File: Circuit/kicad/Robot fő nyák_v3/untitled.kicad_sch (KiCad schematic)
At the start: 0 parts

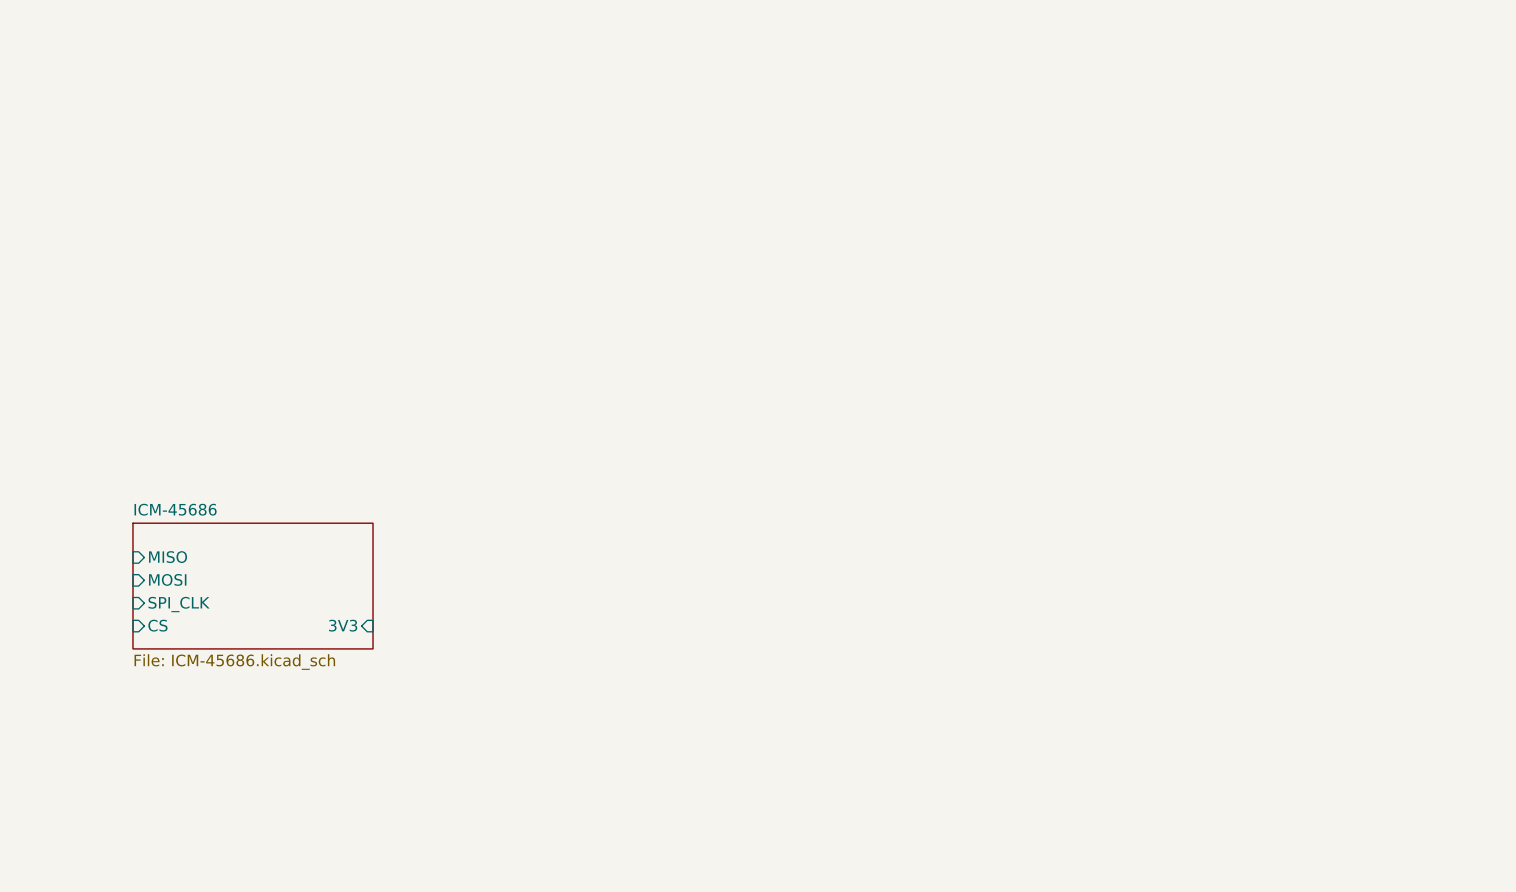
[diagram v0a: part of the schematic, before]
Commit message: kicad bugfixs + bno085 + level shifter ics
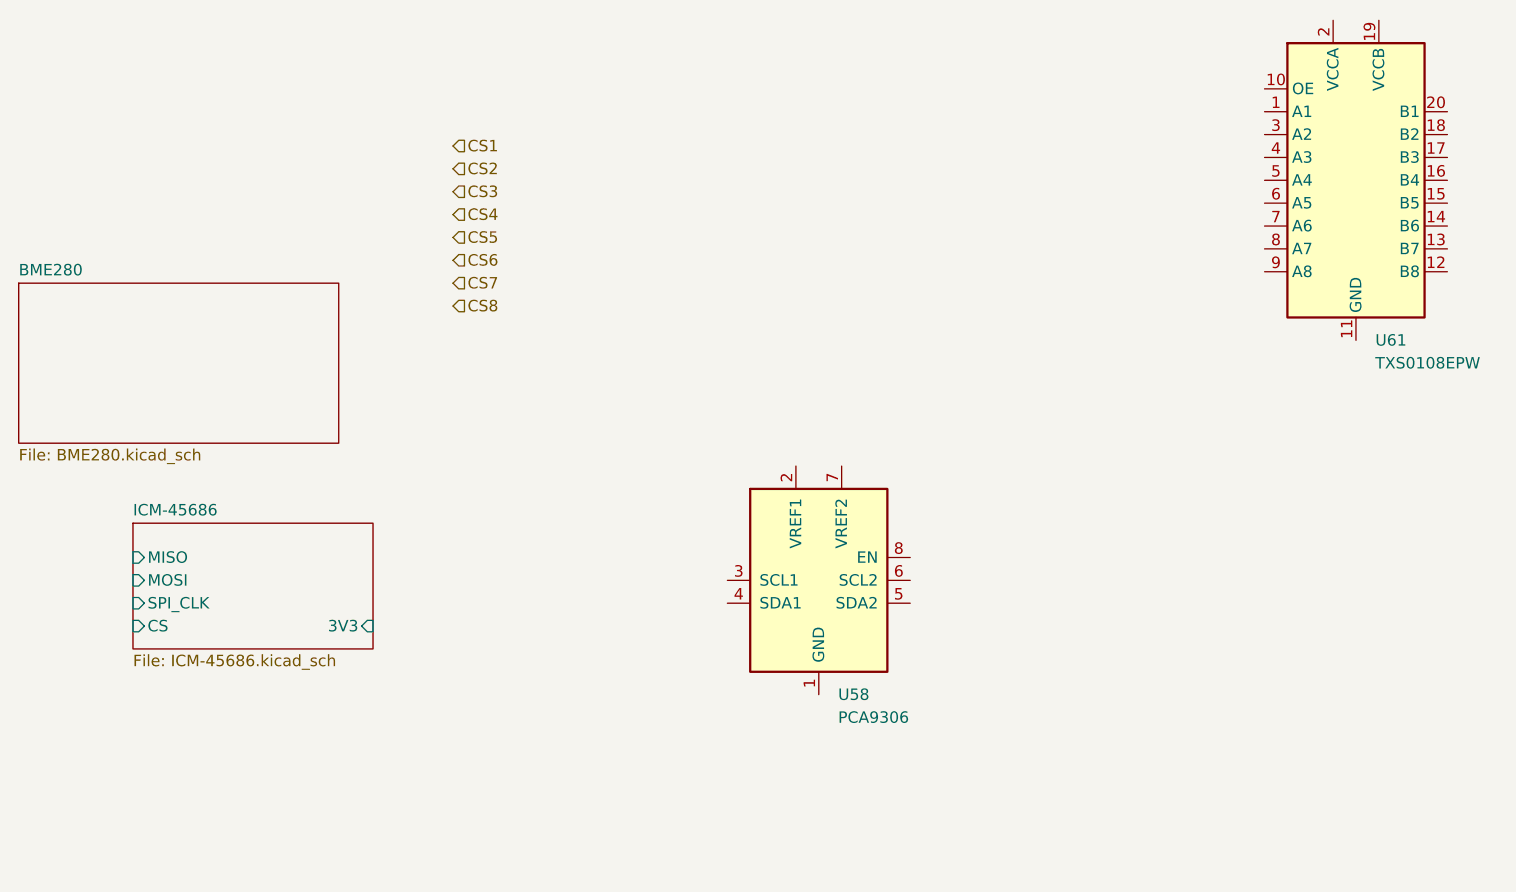
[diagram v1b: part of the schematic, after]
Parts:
- added U58: PCA9306, Package_SO:SSOP-8_2.95x2.8mm_P0.65mm, symbol Interface:PCA9306
- added U61: TXS0108EPW, Package_SO:TSSOP-20_4.4x6.5mm_P0.65mm, symbol Logic_LevelTranslator:TXS0108EPW
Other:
- added sheet BME280 (BME280.kicad_sch)

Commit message: pcb update
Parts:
- removed U58: PCA9306, Package_SO:SSOP-8_2.95x2.8mm_P0.65mm, symbol Interface:PCA9306
- added JP1, JP2: HEADER-1X670MIL, CM5IO:1X06_ROUND_70, symbol CM5IO-eagle-import:HEADER-1X670MIL
- added Q3: BSS138, CM5IO:SOT363, symbol CM5IO-eagle-import:MOSFET-N_DUAL
- added R80, R9, R99: 10K, CM5IO:RESPACK_4X0603, symbol CM5IO-eagle-import:RESISTOR_4PACK
- added SJ1: PS1, CM5IO:SOLDERJUMPER_ARROW_NOPASTE, symbol CM5IO-eagle-import:SOLDERJUMPER
- added SJ2: PS0, CM5IO:SOLDERJUMPER_ARROW_NOPASTE, symbol CM5IO-eagle-import:SOLDERJUMPER
- added U59: 74AHC4050, CM5IO:TSSOP16, symbol CM5IO-eagle-import:74HC4050DTSSOP
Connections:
- new net 3.3V: JP1.2, Q3.2 (G), Q3.5 (G), R99.3 (1), R99.5 (2), U59.1 (VCC)
- new net BOOT: JP2.1, R9.3 (1), U59.7 (3A)
- new net BOOT_3V: U59.6 (3Y)
- new net CS: JP2.6, R80.1, U59.9 (4A)
- new net CS_3V: U59.10 (4Y)
- new net GND: JP1.3, R9.7 (2), R9.8 (2), R99.2 (1), U59.8 (GND)
- new net INT: JP1.6
- new net MOSI: JP2.5, R99.7 (2), U59.11 (5A)
- new net MOSI_3V: U59.12 (5Y)
- new net PS0: JP2.2, R9.2 (1), SJ2.2, U59.3 (1A)
- new net PS0_3V: U59.2 (1Y)
- new net PS1: JP2.3, R9.1, SJ1.2, U59.5 (2A)
- new net PS1_3V: U59.4 (2Y)
- new net RST: JP2.4, R80.2 (1), U59.14 (6A)
- new net RST_3V: U59.15 (6Y)
- new net SCL/SCK/RX: JP1.4, Q3.6 (D), R80.4 (1)
- new net SCL_3V: Q3.1 (S), R99.4 (1)
- new net SDA/MISO/TX: JP1.5, Q3.3 (D), R80.3 (1)
- new net SDA_3V: Q3.4 (S), R99.6 (2)
- new net VCC: JP1.1, R80.5 (2), R80.6 (2), R80.7 (2), R80.8 (2), R9.6 (2), SJ1.1, SJ2.1
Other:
- sheet BMO085 ports: added 3V3, CS, MISO, MOSI, RST, SPI_CLK; removed none
- note added: "Close PS1 for UART Close PS1 and PS0 for SPI"
- note added: "D"
- note added: "Default Bus = I2C"
- note added: "G"
- note added: "I2C Pullups & Shift"
- note added: "S"
- note added: "SA0 is default low, so I2C ADDR = 1001010 (0x4A)"

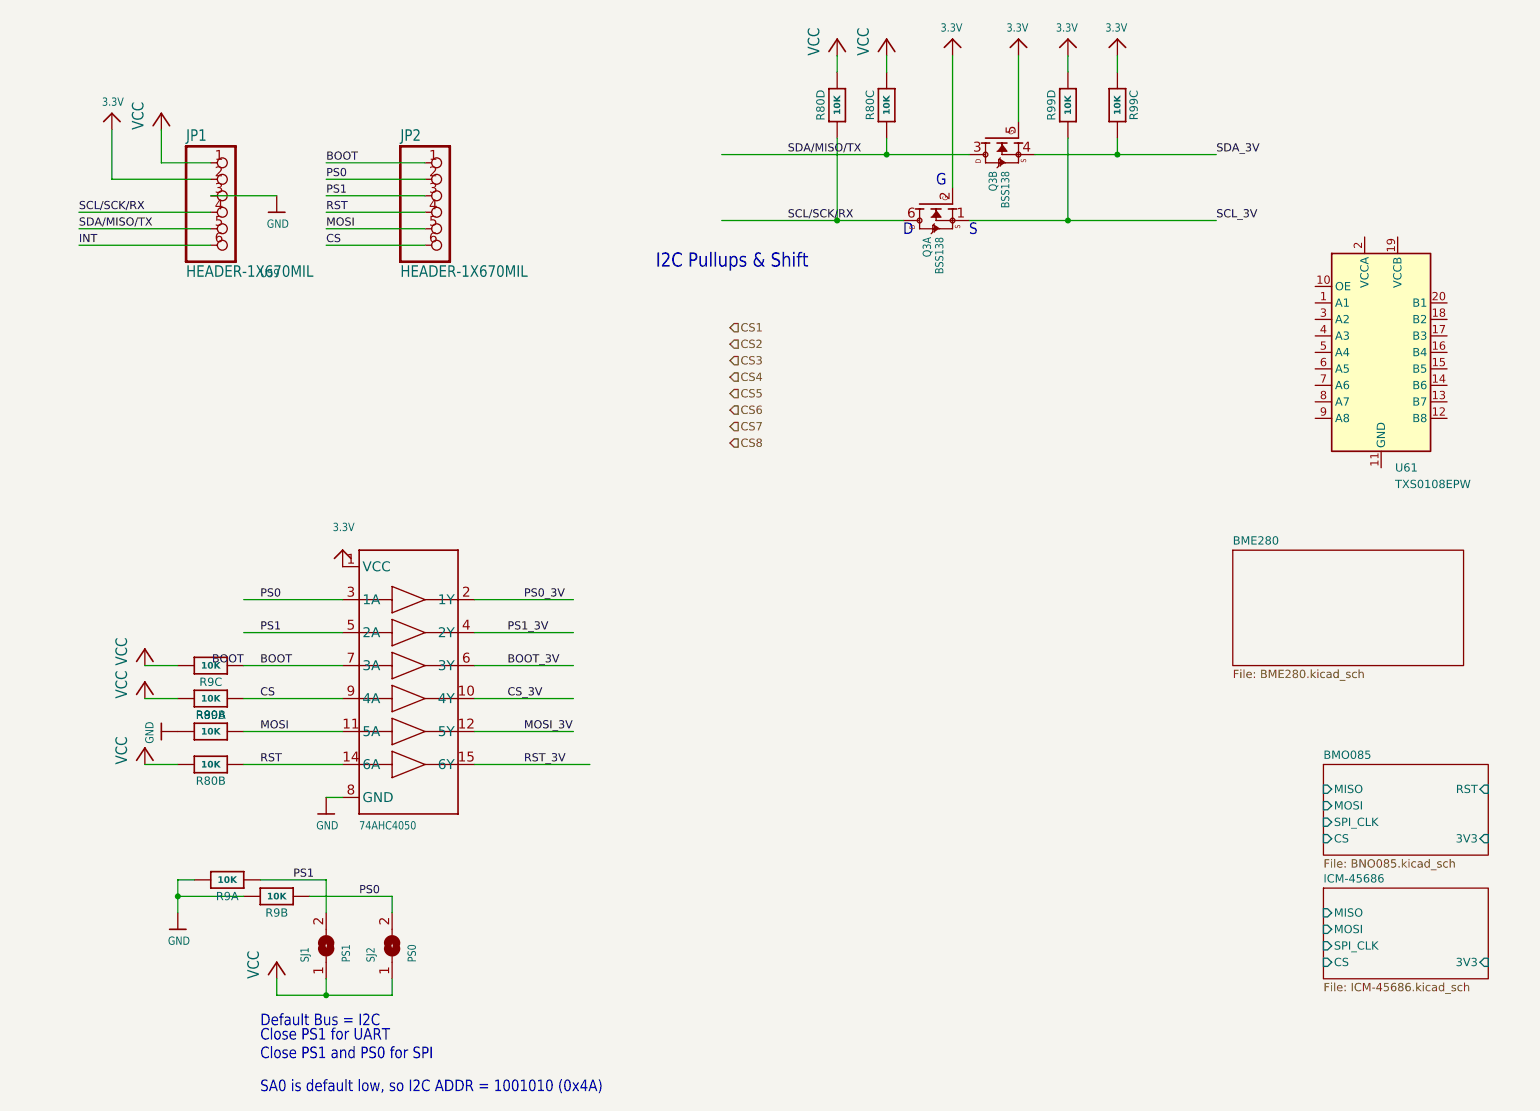
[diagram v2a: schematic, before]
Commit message: KICAD V3.01 Cleaned sheets + update + szekér modell add
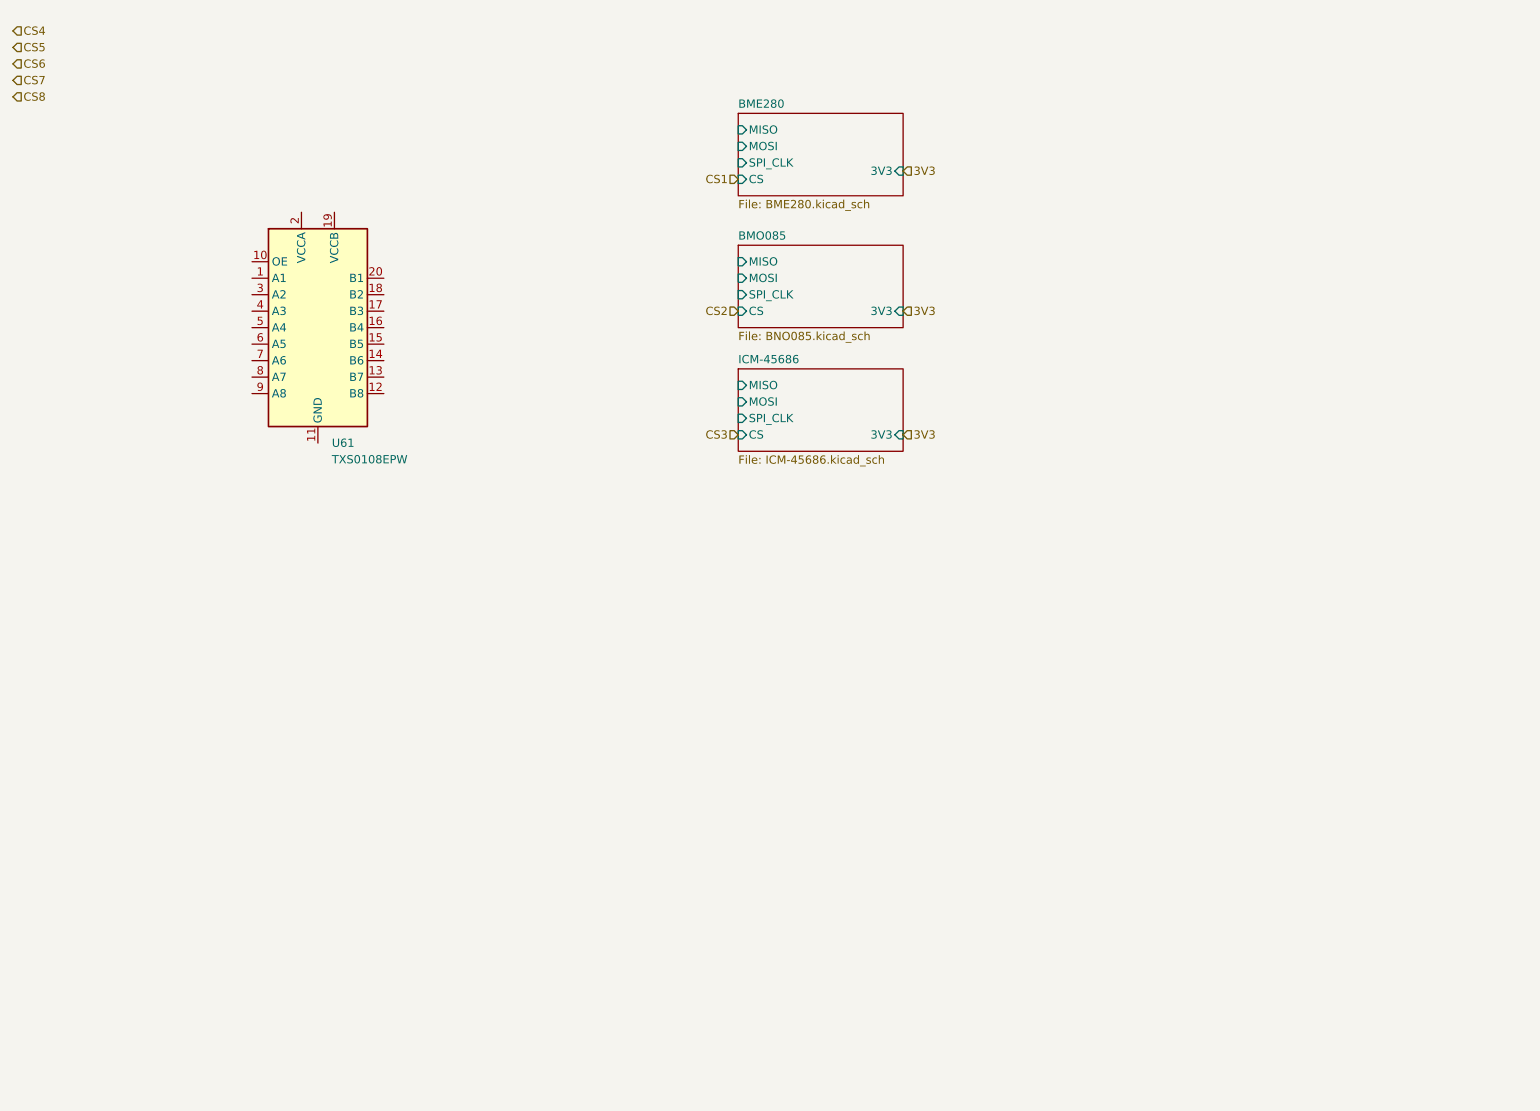
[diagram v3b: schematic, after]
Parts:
- removed JP1, JP2: HEADER-1X670MIL, CM5IO:1X06_ROUND_70, symbol CM5IO-eagle-import:HEADER-1X670MIL
- removed Q3: BSS138, CM5IO:SOT363, symbol CM5IO-eagle-import:MOSFET-N_DUAL
- removed R80, R9, R99: 10K, CM5IO:RESPACK_4X0603, symbol CM5IO-eagle-import:RESISTOR_4PACK
- removed SJ1: PS1, CM5IO:SOLDERJUMPER_ARROW_NOPASTE, symbol CM5IO-eagle-import:SOLDERJUMPER
- removed SJ2: PS0, CM5IO:SOLDERJUMPER_ARROW_NOPASTE, symbol CM5IO-eagle-import:SOLDERJUMPER
- removed U59: 74AHC4050, CM5IO:TSSOP16, symbol CM5IO-eagle-import:74HC4050DTSSOP
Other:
- sheet BME280 ports: added 3V3, CS, MISO, MOSI, SPI_CLK; removed none
- sheet BMO085 ports: added none; removed RST
- note removed: "Close PS1 for UART Close PS1 and PS0 for SPI"
- note removed: "D"
- note removed: "Default Bus = I2C"
- note removed: "G"
- note removed: "I2C Pullups & Shift"
- note removed: "S"
- note removed: "SA0 is default low, so I2C ADDR = 1001010 (0x4A)"
- moved on the sheet: U61

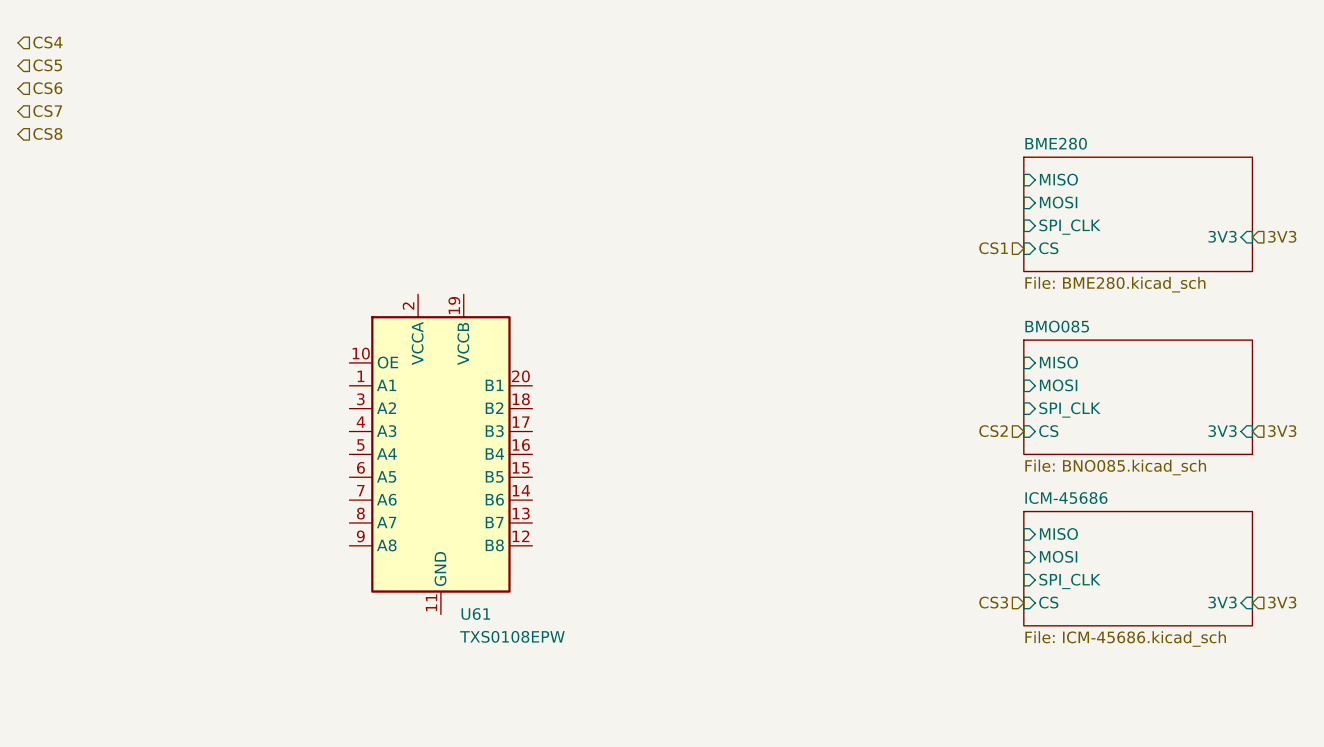
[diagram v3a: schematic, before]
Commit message: Kicad update: power rails v1.0, todo: hc-sr-04  as6500 ic review shift registers change to MCP23S17_SO
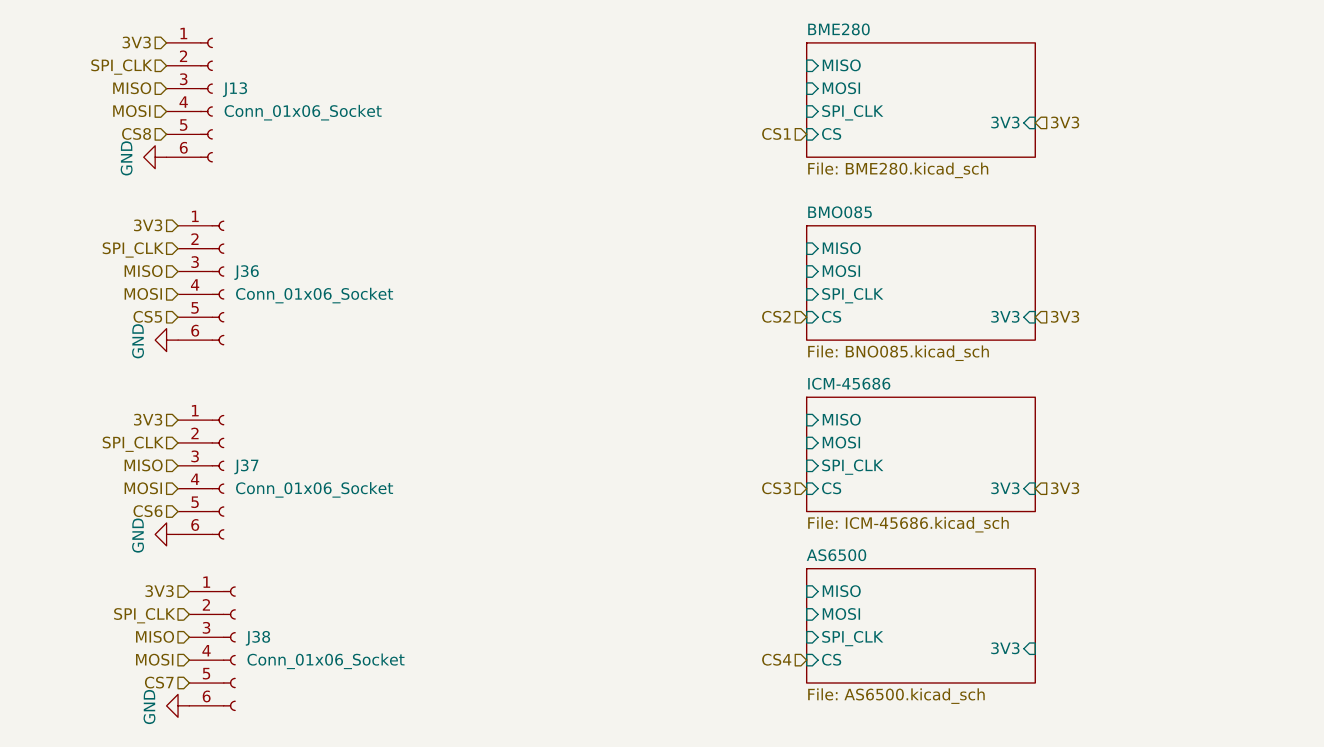
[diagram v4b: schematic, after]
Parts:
- removed U61: TXS0108EPW, Package_SO:TSSOP-20_4.4x6.5mm_P0.65mm, symbol Logic_LevelTranslator:TXS0108EPW
- added J13, J36, J37, J38: Conn_01x06_Socket, symbol Connector:Conn_01x06_Socket
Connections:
- net 3V3: now also J13.1 (Pin_1), J36.1 (Pin_1), J37.1 (Pin_1), J38.1 (Pin_1)
- net CS5: now also J36.5 (Pin_5)
- net CS6: now also J37.5 (Pin_5)
- net CS7: now also J38.5 (Pin_5)
- net CS8: now also J13.5 (Pin_5)
- new net GND: J13.6 (Pin_6), J36.6 (Pin_6), J37.6 (Pin_6), J38.6 (Pin_6)
- new net MISO: J13.3 (Pin_3), J36.3 (Pin_3), J37.3 (Pin_3), J38.3 (Pin_3)
- new net MOSI: J13.4 (Pin_4), J36.4 (Pin_4), J37.4 (Pin_4), J38.4 (Pin_4)
- new net SPI_CLK: J13.2 (Pin_2), J36.2 (Pin_2), J37.2 (Pin_2), J38.2 (Pin_2)
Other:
- added sheet AS6500 (AS6500.kicad_sch)
